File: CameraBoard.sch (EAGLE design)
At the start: 17 parts

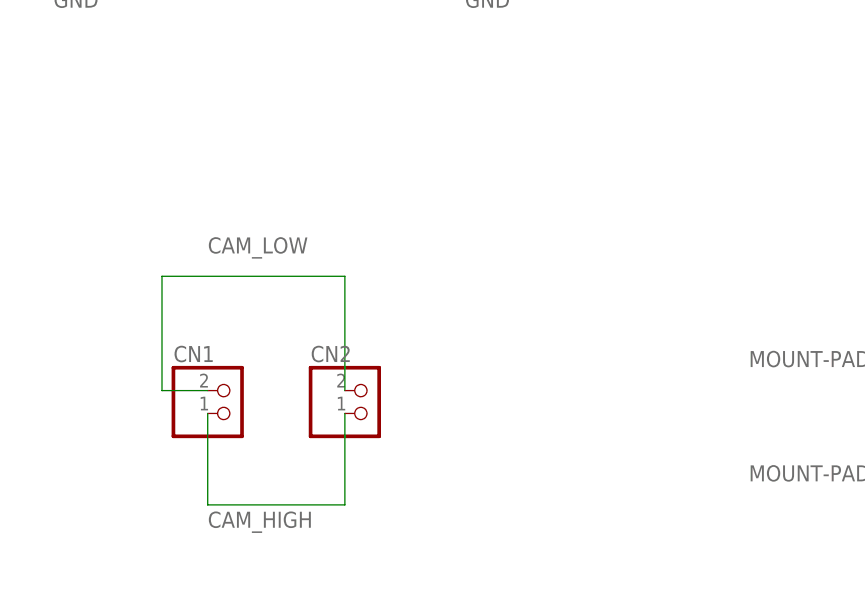
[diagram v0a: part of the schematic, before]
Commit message: Removed JSTs, updated revision
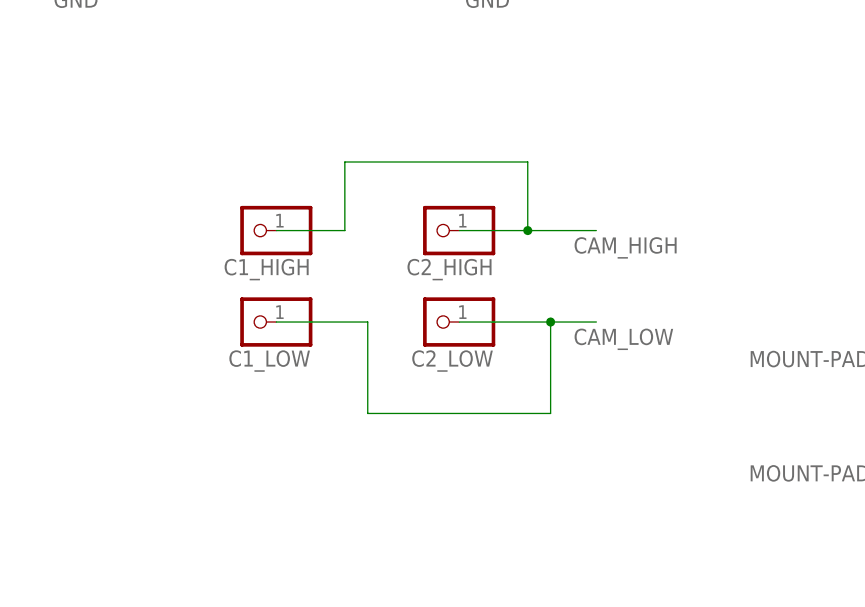
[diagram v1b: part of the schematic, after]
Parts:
- removed CN1, CN2: (no value), adafruit:JST_2PIN-SMT-RA
- added C1_HIGH, C1_LOW, C2_HIGH, C2_LOW: (no value), adafruit:PINHD-1X1
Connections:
- net CAM_HIGH: now also C1_HIGH.1, C2_HIGH.1; no longer CN1.2, CN2.2
- net CAM_LOW: now also C1_LOW.1, C2_LOW.1; no longer CN1.1, CN2.1
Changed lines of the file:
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@@
 <?xml version="1.0" encoding="utf-8"?>
 <!DOCTYPE eagle SYSTEM "eagle.dtd">
-<eagle version="9.3.1">
+<eagle version="9.4.1">
 <drawing>
 <settings>
@@
 <part name="GND4" library="supply2" library_urn="urn:adsk.eagle:library:372" deviceset="GND" device=""/>
 <part name="SUPPLY3" library="supply2" library_urn="urn:adsk.eagle:library:372" deviceset="GND" device=""/>
-<part name="CN1" library="adafruit" library_urn="urn:adsk.eagle:library:420" deviceset="JST_2PIN" device="-SMT-RA" package3d_urn="urn:adsk.eagle:package:6240692/1"/>
-<part name="CN2" library="adafruit" library_urn="urn:adsk.eagle:library:420" deviceset="JST_2PIN" device="-SMT-RA" package3d_urn="urn:adsk.eagle:package:6240692/1"/>
 <part name="H1" library="holes" library_urn="urn:adsk.eagle:library:237" deviceset="MOUNT-PAD-ROUND" device="2.8" package3d_urn="urn:adsk.eagle:package:14281/1"/>
 <part name="H2" library="holes" library_urn="urn:adsk.eagle:library:237" deviceset="MOUNT-PAD-ROUND" device="2.8" package3d_urn="urn:adsk.eagle:package:14281/1"/>
@@
 <part name="H5" library="holes" library_urn="urn:adsk.eagle:library:237" deviceset="MOUNT-PAD-ROUND" device="2.8" package3d_urn="urn:adsk.eagle:package:14281/1"/>
 <part name="H6" library="holes" library_urn="urn:adsk.eagle:library:237" deviceset="MOUNT-PAD-ROUND" device="2.8" package3d_urn="urn:adsk.eagle:package:14281/1"/>
+<part name="C1_HIGH" library="adafruit" library_urn="urn:adsk.eagle:library:420" deviceset="PINHD-1X1" device=""/>
+<part name="C1_LOW" library="adafruit" library_urn="urn:adsk.eagle:library:420" deviceset="PINHD-1X1" device=""/>
+<part name="C2_HIGH" library="adafruit" library_urn="urn:adsk.eagle:library:420" deviceset="PINHD-1X1" device=""/>
+<part name="C2_LOW" library="adafruit" library_urn="urn:adsk.eagle:library:420" deviceset="PINHD-1X1" device=""/>
 </parts>
 <sheets>
@@
 <attribute name="VALUE" x="-78.105" y="19.685" size="1.778" layer="96"/>
 </instance>
-<instance part="CN1" gate="G$1" x="-43.18" y="-22.86" smashed="yes">
-<attribute name="NAME" x="-49.53" y="-17.145" size="1.778" layer="95"/>
-<attribute name="VALUE" x="-49.53" y="-27.94" size="1.778" layer="96"/>
-</instance>
-<instance part="CN2" gate="G$1" x="-27.94" y="-22.86" smashed="yes">
-<attribute name="NAME" x="-34.29" y="-17.145" size="1.778" layer="95"/>
-<attribute name="VALUE" x="-34.29" y="-27.94" size="1.778" layer="96"/>
-</instance>
 <instance part="H1" gate="G$1" x="63.5" y="-27.94" smashed="yes">
 <attribute name="NAME" x="66.294" y="-27.3558" size="1.778" layer="95"/>
@@
 <attribute name="NAME" x="-89.154" y="-29.8958" size="1.778" layer="95"/>
 <attribute name="VALUE" x="-89.154" y="-32.9438" size="1.778" layer="96" rot="MR0"/>
+</instance>
+<instance part="C1_HIGH" gate="G$1" x="-40.64" y="-2.54" smashed="yes" rot="R180">
+<attribute name="NAME" x="-34.29" y="-5.715" size="1.778" layer="95" rot="R180"/>
+<attribute name="VALUE" x="-34.29" y="2.54" size="1.778" layer="96" rot="R180"/>
+</instance>
+<instance part="C1_LOW" gate="G$1" x="-40.64" y="-12.7" smashed="yes" rot="R180">
+<attribute name="NAME" x="-34.29" y="-15.875" size="1.778" layer="95" rot="R180"/>
+<attribute name="VALUE" x="-34.29" y="-7.62" size="1.778" layer="96" rot="R180"/>
+</instance>
+<instance part="C2_HIGH" gate="G$1" x="-20.32" y="-2.54" smashed="yes" rot="R180">
+<attribute name="NAME" x="-13.97" y="-5.715" size="1.778" layer="95" rot="R180"/>
+<attribute name="VALUE" x="-13.97" y="2.54" size="1.778" layer="96" rot="R180"/>
+</instance>
+<instance part="C2_LOW" gate="G$1" x="-20.32" y="-12.7" smashed="yes" rot="R180">
+<attribute name="NAME" x="-13.97" y="-15.875" size="1.778" layer="95" rot="R180"/>
+<attribute name="VALUE" x="-13.97" y="-7.62" size="1.778" layer="96" rot="R180"/>
 </instance>
 </instances>
@@
 </segment>
 <segment>
-<pinref part="CN1" gate="G$1" pin="1"/>
-<wire x1="-45.72" y1="-20.32" x2="-50.8" y2="-20.32" width="0.1524" layer="91"/>
-<wire x1="-50.8" y1="-20.32" x2="-50.8" y2="-7.62" width="0.1524" layer="91"/>
-<wire x1="-50.8" y1="-7.62" x2="-30.48" y2="-7.62" width="0.1524" layer="91"/>
-<pinref part="CN2" gate="G$1" pin="1"/>
-<wire x1="-30.48" y1="-7.62" x2="-30.48" y2="-20.32" width="0.1524" layer="91"/>
-<label x="-45.72" y="-5.08" size="1.778" layer="95"/>
+<pinref part="C1_LOW" gate="G$1" pin="1"/>
+<wire x1="-38.1" y1="-12.7" x2="-27.94" y2="-12.7" width="0.1524" layer="91"/>
+<wire x1="-27.94" y1="-12.7" x2="-27.94" y2="-22.86" width="0.1524" layer="91"/>
+<wire x1="-27.94" y1="-22.86" x2="-7.62" y2="-22.86" width="0.1524" layer="91"/>
+<pinref part="C2_LOW" gate="G$1" pin="1"/>
+<wire x1="-7.62" y1="-22.86" x2="-7.62" y2="-12.7" width="0.1524" layer="91"/>
+<wire x1="-7.62" y1="-12.7" x2="-17.78" y2="-12.7" width="0.1524" layer="91"/>
+<wire x1="-7.62" y1="-12.7" x2="-2.54" y2="-12.7" width="0.1524" layer="91"/>
+<junction x="-7.62" y="-12.7"/>
+<label x="-5.08" y="-15.24" size="1.778" layer="95"/>
 </segment>
 </net>
@@
 </segment>
 <segment>
-<pinref part="CN2" gate="G$1" pin="2"/>
-<wire x1="-30.48" y1="-22.86" x2="-30.48" y2="-33.02" width="0.1524" layer="91"/>
-<wire x1="-30.48" y1="-33.02" x2="-45.72" y2="-33.02" width="0.1524" layer="91"/>
-<pinref part="CN1" gate="G$1" pin="2"/>
-<wire x1="-45.72" y1="-33.02" x2="-45.72" y2="-22.86" width="0.1524" layer="91"/>
-<label x="-45.72" y="-35.56" size="1.778" layer="95"/>
-</segment>
-</net>
+<pinref part="C1_HIGH" gate="G$1" pin="1"/>
+<wire x1="-38.1" y1="-2.54" x2="-30.48" y2="-2.54" width="0.1524" layer="91"/>
+<wire x1="-30.48" y1="-2.54" x2="-30.48" y2="5.08" width="0.1524" layer="91"/>
+<wire x1="-30.48" y1="5.08" x2="-10.16" y2="5.08" width="0.1524" layer="91"/>
+<wire x1="-10.16" y1="5.08" x2="-10.16" y2="-2.54" width="0.1524" layer="91"/>
+<pinref part="C2_HIGH" gate="G$1" pin="1"/>
+<wire x1="-10.16" y1="-2.54" x2="-17.78" y2="-2.54" width="0.1524" layer="91"/>
+<wire x1="-10.16" y1="-2.54" x2="-2.54" y2="-2.54" width="0.1524" layer="91"/>
+<junction x="-10.16" y="-2.54"/>
+<label x="-5.08" y="-5.08" size="1.778" layer="95"/>
+</segment>
+</net>
